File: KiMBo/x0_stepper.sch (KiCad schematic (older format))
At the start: 25 parts, among them U14 TMC2130

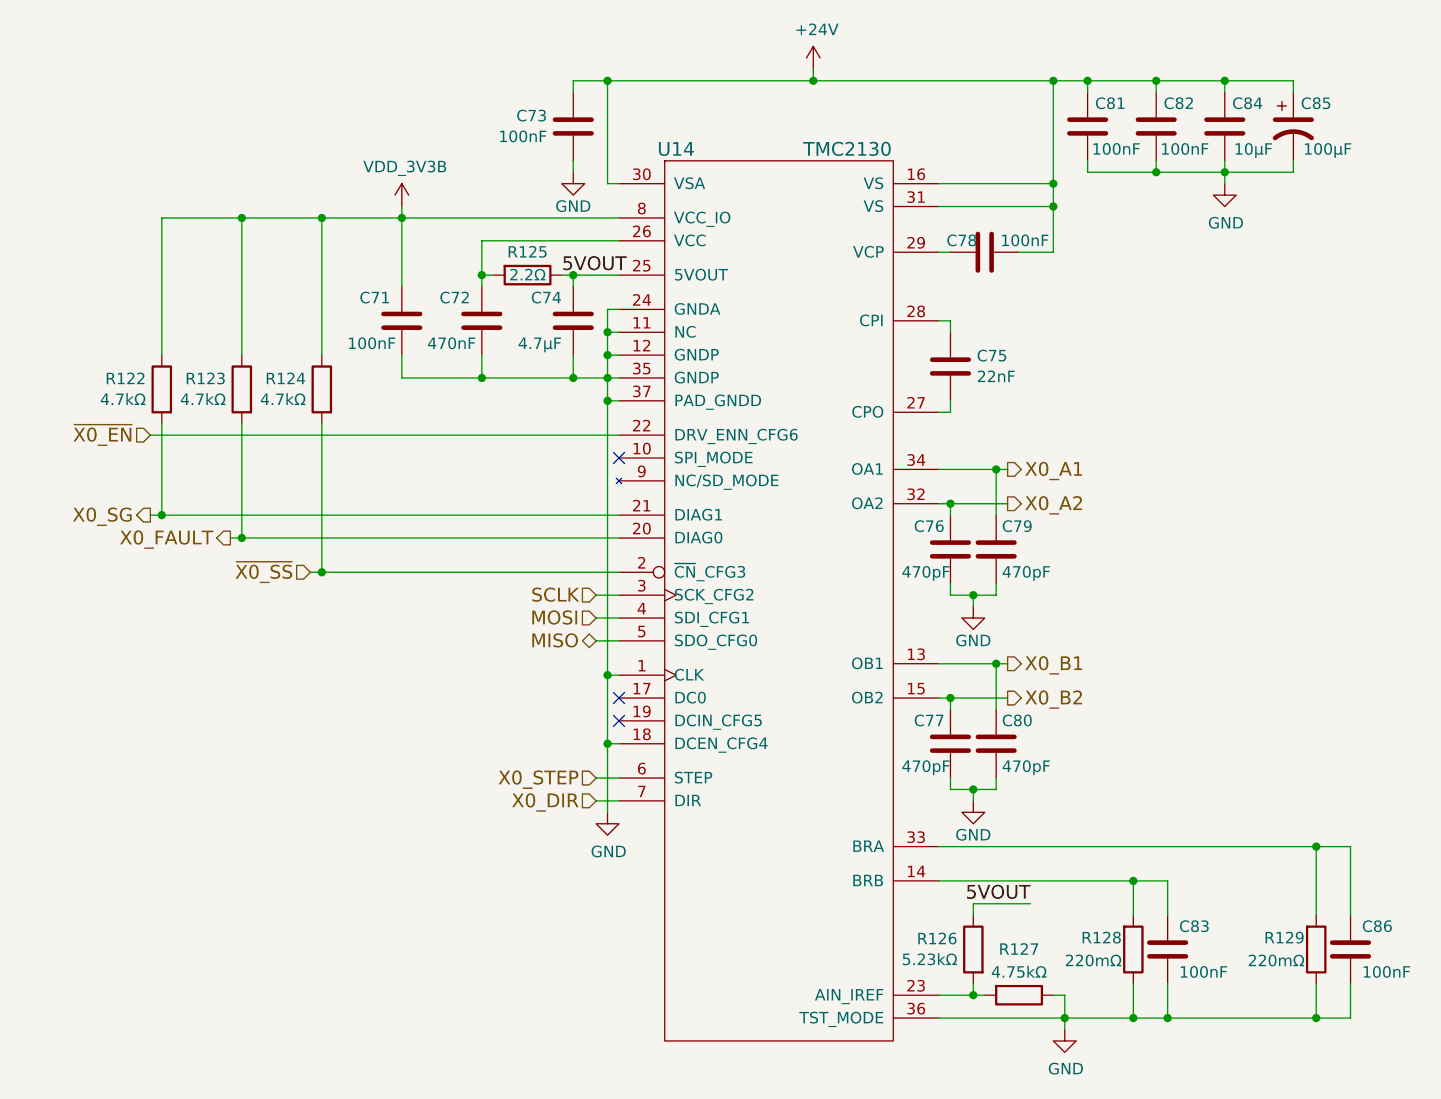
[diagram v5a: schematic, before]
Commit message: Remove the unneeded oscillator, track down which components are underneath the OSD3358 and put them on the top
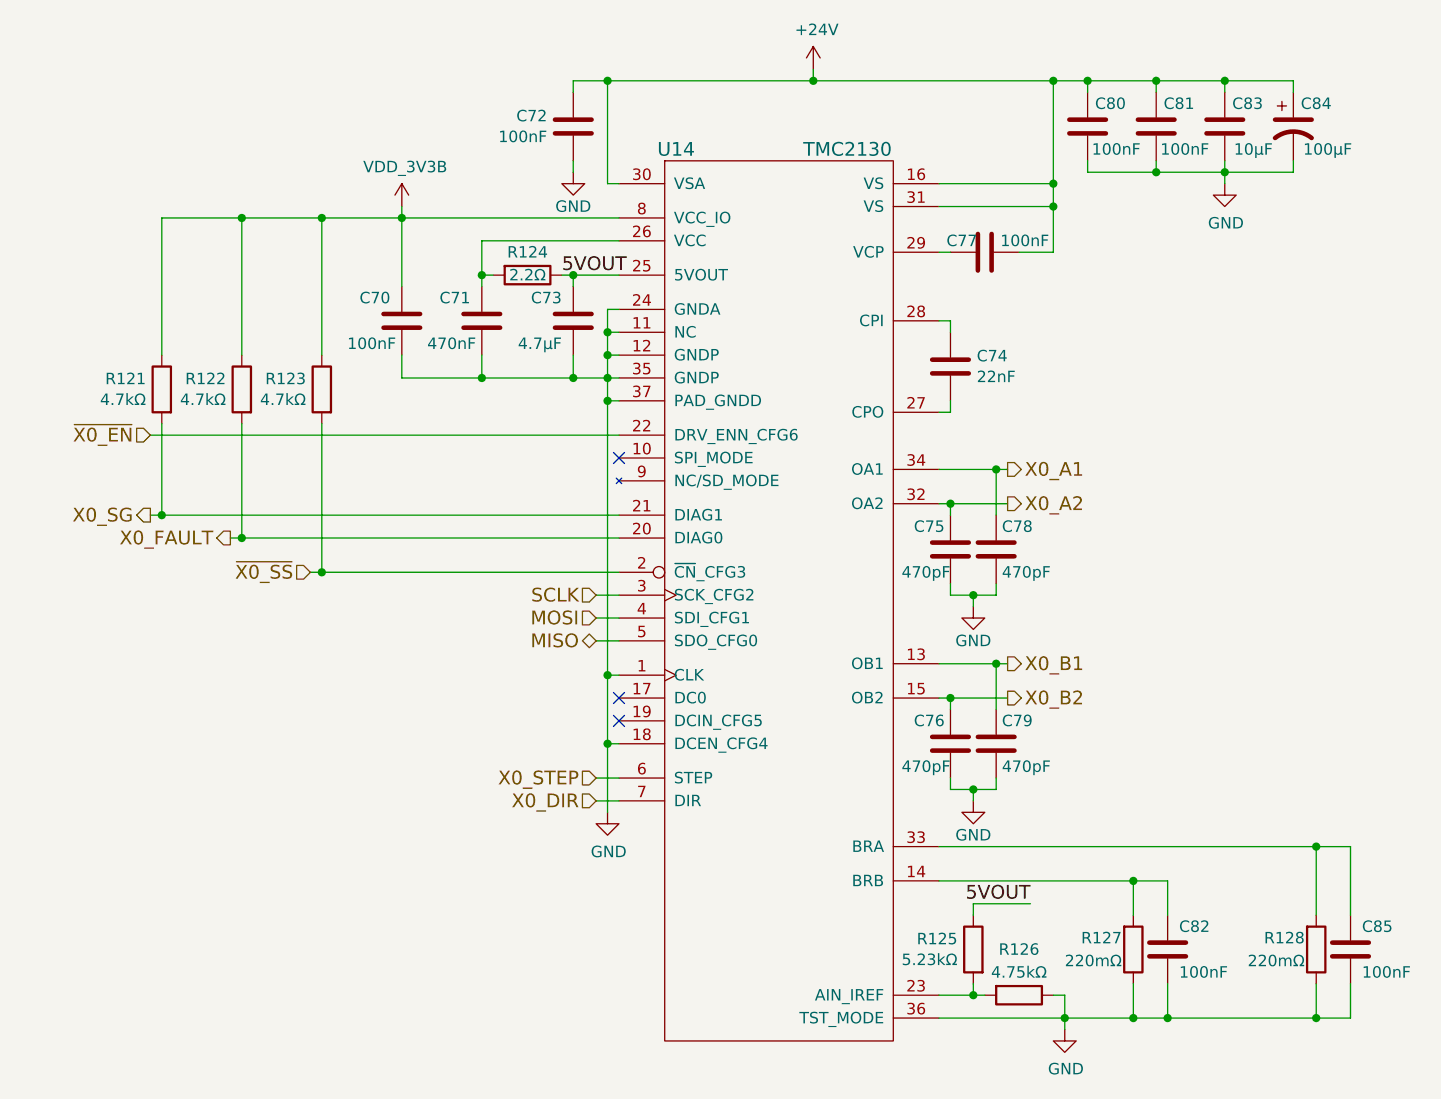
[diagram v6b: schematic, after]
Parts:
- renumbered C71 to C70, C72 to C71, C73 to C72, C74 to C73, C75 to C74, C76 to C75, C77 to C76, C78 to C77, C79 to C78, C80 to C79, C81 to C80, C82 to C81, C83 to C82, C84 to C83, C85 to C84, C86 to C85, R122 to R121, R123 to R122, R124 to R123, R125 to R124, R126 to R125, R127 to R126, R128 to R127, R129 to R128
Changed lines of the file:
@@
 X0_SG
 $Comp
-L C C73
+L C C72
 U 1 1 5BA7E13B
 P 7500 3100
-F 0 "C73" H 7386 3054 50  0000 R CNN
+F 0 "C72" H 7386 3054 50  0000 R CNN
 F 1 "100nF" H 7386 3145 50  0000 R CNN
 F 2 "Capacitors_SMD:C_0603" H 7538 2950 50  0001 C CNN
@@
 $EndComp
 $Comp
-L C C78
+L C C77
 U 1 1 5BA7E13C
 P 9300 3650
-F 0 "C78" V 9250 3550 50  0000 C CNN
+F 0 "C77" V 9250 3550 50  0000 C CNN
 F 1 "100nF" V 9250 3825 50  0000 C CNN
 F 2 "Capacitors_SMD:C_0603" H 9338 3500 50  0001 C CNN
@@
 $EndComp
 $Comp
-L CP1 C85
+L CP1 C84
 U 1 1 58C092C4
 P 10650 3100
-F 0 "C85" H 10750 3200 50  0000 C CNN
+F 0 "C84" H 10750 3200 50  0000 C CNN
 F 1 "100μF" H 10800 3000 50  0000 C CNN
 F 2 "Capacitors_SMD:c_elec_8x10" H 10650 3100 50  0001 C CNN
@@
 $EndComp
 $Comp
-L C C81
+L C C80
 U 1 1 58C092CB
 P 9750 3100
-F 0 "C81" H 9650 3200 50  0000 C CNN
+F 0 "C80" H 9650 3200 50  0000 C CNN
 F 1 "100nF" H 9625 3000 50  0000 C CNN
 F 2 "Capacitors_SMD:C_0603" H 9788 2950 50  0001 C CNN
@@
 $EndComp
 $Comp
-L GND #PWR0172
+L GND #PWR0170
 U 1 1 58C092D2
 P 7500 3300
-F 0 "#PWR0172" H 7500 3050 50  0001 C CNN
+F 0 "#PWR0170" H 7500 3050 50  0001 C CNN
 F 1 "GND" H 7500 3150 50  0000 C CNN
 F 2 "" H 7500 3300 50  0000 C CNN
@@
 $EndComp
 $Comp
-L C C82
+L C C81
 U 1 1 5BA7E140
 P 10050 3100
-F 0 "C82" H 9950 3200 50  0000 C CNN
+F 0 "C81" H 9950 3200 50  0000 C CNN
 F 1 "100nF" H 9925 3000 50  0000 C CNN
 F 2 "Capacitors_SMD:C_0603" H 10088 2950 50  0001 C CNN
@@
 $EndComp
 $Comp
-L GND #PWR0173
+L GND #PWR0171
 U 1 1 5BA7E141
 P 10350 3350
-F 0 "#PWR0173" H 10350 3100 50  0001 C CNN
+F 0 "#PWR0171" H 10350 3100 50  0001 C CNN
 F 1 "GND" H 10355 3177 50  0000 C CNN
 F 2 "" H 10350 3350 50  0000 C CNN
@@
 $EndComp
 $Comp
-L +24V #PWR0174
+L +24V #PWR0172
 U 1 1 58C092E5
 P 8550 2850
-F 0 "#PWR0174" H 8550 2700 50  0001 C CNN
+F 0 "#PWR0172" H 8550 2700 50  0001 C CNN
 F 1 "+24V" H 8565 3023 50  0000 C CNN
 F 2 "" H 8550 2850 50  0000 C CNN
@@
 $EndComp
 $Comp
-L C C75
+L C C74
 U 1 1 58C092EB
 P 9150 4150
-F 0 "C75" H 9265 4196 50  0000 L CNN
+F 0 "C74" H 9265 4196 50  0000 L CNN
 F 1 "22nF" H 9265 4105 50  0000 L CNN
 F 2 "Capacitors_SMD:C_0603" H 9188 4000 50  0001 C CNN
@@
 $EndComp
 $Comp
-L R R129
+L R R128
 U 1 1 58C092F2
 P 10750 6700
-F 0 "R129" H 10700 6650 50  0000 R CNN
+F 0 "R128" H 10700 6650 50  0000 R CNN
 F 1 "220mΩ" H 10700 6750 50  0000 R CNN
 F 2 "Resistors_SMD:R_0805" V 10680 6700 50  0001 C CNN
@@
 $EndComp
 $Comp
-L R R128
+L R R127
 U 1 1 58C092F9
 P 9950 6700
-F 0 "R128" H 9900 6650 50  0000 R CNN
+F 0 "R127" H 9900 6650 50  0000 R CNN
 F 1 "220mΩ" H 9900 6750 50  0000 R CNN
 F 2 "Resistors_SMD:R_0805" V 9880 6700 50  0001 C CNN
@@
 $EndComp
 $Comp
-L GND #PWR0175
+L GND #PWR0173
 U 1 1 5BA7E146
 P 9650 7050
-F 0 "#PWR0175" H 9650 6800 50  0001 C CNN
+F 0 "#PWR0173" H 9650 6800 50  0001 C CNN
 F 1 "GND" H 9655 6877 50  0000 C CNN
 F 2 "" H 9650 7050 50  0000 C CNN
@@
 NoConn ~ 7700 5600
 $Comp
-L R R125
+L R R124
 U 1 1 5BA7E147
 P 7300 3750
-F 0 "R125" V 7200 3750 50  0000 C CNN
+F 0 "R124" V 7200 3750 50  0000 C CNN
 F 1 "2.2Ω" V 7300 3750 50  0000 C CNN
 F 2 "Resistors_SMD:R_0603" V 7230 3750 50  0001 C CNN
@@
 $EndComp
 $Comp
-L C C72
+L C C71
 U 1 1 5BA7E148
 P 7100 3950
-F 0 "C72" H 7150 4050 50  0000 L CNN
+F 0 "C71" H 7150 4050 50  0000 L CNN
 F 1 "470nF" H 7125 3850 50  0000 L CNN
 F 2 "Capacitors_SMD:C_0603" H 7138 3800 50  0001 C CNN
@@
 NoConn ~ 7700 5700
 $Comp
-L GND #PWR0176
+L GND #PWR0174
 U 1 1 5BA7E149
 P 7650 6100
-F 0 "#PWR0176" H 7650 5850 50  0001 C CNN
+F 0 "#PWR0174" H 7650 5850 50  0001 C CNN
 F 1 "GND" H 7655 5927 50  0000 C CNN
 F 2 "" H 7650 6100 50  0000 C CNN
@@
 $EndComp
 $Comp
-L C C83
+L C C82
 U 1 1 5BA7E14A
 P 10100 6700
-F 0 "C83" H 10150 6800 50  0000 L CNN
+F 0 "C82" H 10150 6800 50  0000 L CNN
 F 1 "100nF" H 10150 6600 50  0000 L CNN
 F 2 "Capacitors_SMD:C_0603" H 10138 6550 50  0001 C CNN
@@
 X0_FAULT
 $Comp
-L R R123
+L R R122
 U 1 1 58C09331
 P 6050 4250
-F 0 "R123" H 6119 4296 50  0000 L CNN
+F 0 "R122" H 6119 4296 50  0000 L CNN
 F 1 "4.7kΩ" H 6119 4205 50  0000 L CNN
 F 2 "Resistors_SMD:R_0603" V 5980 4250 50  0001 C CNN
@@
 NoConn ~ 7700 4550
 $Comp
-L C C74
+L C C73
 U 1 1 5BA7E14C
 P 7500 3950
-F 0 "C74" H 7550 4050 50  0000 L CNN
+F 0 "C73" H 7550 4050 50  0000 L CNN
 F 1 "4.7μF" H 7550 3850 50  0000 L CNN
 F 2 "Capacitors_SMD:C_0603" H 7538 3800 50  0001 C CNN
@@
 5VOUT
 $Comp
-L R R126
+L R R125
 U 1 1 5BA7E14D
 P 9250 6700
-F 0 "R126" H 9319 6746 50  0000 L CNN
+F 0 "R125" H 9319 6746 50  0000 L CNN
 F 1 "5.23kΩ" H 9319 6655 50  0000 L CNN
 F 2 "Resistors_SMD:R_0603" V 9180 6700 50  0001 C CNN
@@
 5VOUT
 $Comp
-L R R127
+L R R126
 U 1 1 5BA7E14E
 P 9450 6900
-F 0 "R127" V 9250 6900 50  0000 C CNN
+F 0 "R126" V 9250 6900 50  0000 C CNN
 F 1 "4.75kΩ" V 9350 6900 50  0000 C CNN
 F 2 "Resistors_SMD:R_0603" V 9380 6900 50  0001 C CNN
@@
 $EndComp
 $Comp
-L R R124
+L R R123
 U 1 1 58C09353
 P 6400 4250
-F 0 "R124" H 6469 4296 50  0000 L CNN
+F 0 "R123" H 6469 4296 50  0000 L CNN
 F 1 "4.7kΩ" H 6469 4205 50  0000 L CNN
 F 2 "Resistors_SMD:R_0603" V 6330 4250 50  0001 C CNN
@@
 $EndComp
 $Comp
-L C C86
+L C C85
 U 1 1 58C0935A
 P 10900 6700
-F 0 "C86" H 10950 6800 50  0000 L CNN
+F 0 "C85" H 10950 6800 50  0000 L CNN
 F 1 "100nF" H 10950 6600 50  0000 L CNN
 F 2 "Capacitors_SMD:C_0603" H 10938 6550 50  0001 C CNN
@@
 $EndComp
 $Comp
-L C C76
+L C C75
 U 1 1 58C09363
 P 9150 4950
-F 0 "C76" H 9175 5050 50  0000 L CNN
+F 0 "C75" H 9175 5050 50  0000 L CNN
 F 1 "470pF" H 9150 4850 50  0000 L CNN
 F 2 "Capacitors_SMD:C_0603" H 9188 4800 50  0001 C CNN
@@
 $EndComp
 $Comp
-L GND #PWR0177
+L GND #PWR0175
 U 1 1 58C0936A
 P 9250 5200
-F 0 "#PWR0177" H 9250 4950 50  0001 C CNN
+F 0 "#PWR0175" H 9250 4950 50  0001 C CNN
 F 1 "GND" H 9250 5050 50  0000 C CNN
 F 2 "" H 9250 5200 50  0000 C CNN
@@
 $EndComp
 $Comp
-L C C79
+L C C78
 U 1 1 58C09370
 P 9350 4950
-F 0 "C79" H 9375 5050 50  0000 L CNN
+F 0 "C78" H 9375 5050 50  0000 L CNN
 F 1 "470pF" H 9375 4850 50  0000 L CNN
 F 2 "Capacitors_SMD:C_0603" H 9388 4800 50  0001 C CNN
@@
 $EndComp
 $Comp
-L C C77
+L C C76
 U 1 1 5BA7E154
 P 9150 5800
-F 0 "C77" H 9175 5900 50  0000 L CNN
+F 0 "C76" H 9175 5900 50  0000 L CNN
 F 1 "470pF" H 9150 5700 50  0000 L CNN
 F 2 "Capacitors_SMD:C_0603" H 9188 5650 50  0001 C CNN
@@
 $EndComp
 $Comp
-L GND #PWR0178
+L GND #PWR0176
 U 1 1 58C0937E
 P 9250 6050
-F 0 "#PWR0178" H 9250 5800 50  0001 C CNN
+F 0 "#PWR0176" H 9250 5800 50  0001 C CNN
 F 1 "GND" H 9250 5900 50  0000 C CNN
 F 2 "" H 9250 6050 50  0000 C CNN
@@
 $EndComp
 $Comp
-L C C80
+L C C79
 U 1 1 58C09384
 P 9350 5800
-F 0 "C80" H 9375 5900 50  0000 L CNN
+F 0 "C79" H 9375 5900 50  0000 L CNN
 F 1 "470pF" H 9375 5700 50  0000 L CNN
 F 2 "Capacitors_SMD:C_0603" H 9388 5650 50  0001 C CNN
@@
 	9150 6000 9150 5950
 $Comp
-L R R122
+L R R121
 U 1 1 5BA7E158
 P 5700 4250
-F 0 "R122" H 5769 4296 50  0000 L CNN
+F 0 "R121" H 5769 4296 50  0000 L CNN
 F 1 "4.7kΩ" H 5769 4205 50  0000 L CNN
 F 2 "Resistors_SMD:R_0603" V 5630 4250 50  0001 C CNN
@@
 Connection ~ 6050 3500
 $Comp
-L C C84
+L C C83
 U 1 1 5BA7E159
 P 10350 3100
-F 0 "C84" H 10250 3200 50  0000 C CNN
+F 0 "C83" H 10250 3200 50  0000 C CNN
 F 1 "10μF" H 10225 3000 50  0000 C CNN
 F 2 "Capacitors_SMD:C_0805" H 10388 2950 50  0001 C CNN
@@
 	5700 3500 7700 3500
 $Comp
-L VDD_3V3B #PWR0179
+L VDD_3V3B #PWR0177
 U 1 1 5A2FF856
 P 6750 3450
-F 0 "#PWR0179" H 6750 3300 50  0001 C CNN
+F 0 "#PWR0177" H 6750 3300 50  0001 C CNN
 F 1 "VDD_3V3B" H 6765 3623 50  0000 C CNN
 F 2 "" H 6750 3450 50  0000 C CNN
@@
 $EndComp
 $Comp
-L C C71
+L C C70
 U 1 1 5A89853C
 P 6750 3950
-F 0 "C71" H 6800 4050 50  0000 L CNN
+F 0 "C70" H 6800 4050 50  0000 L CNN
 F 1 "100nF" H 6775 3850 50  0000 L CNN
 F 2 "Capacitors_SMD:C_0603" H 6788 3800 50  0001 C CNN
